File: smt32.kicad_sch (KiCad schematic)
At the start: 3 parts, among them P1 CONN28, P2 CONN28, P3 CONN6

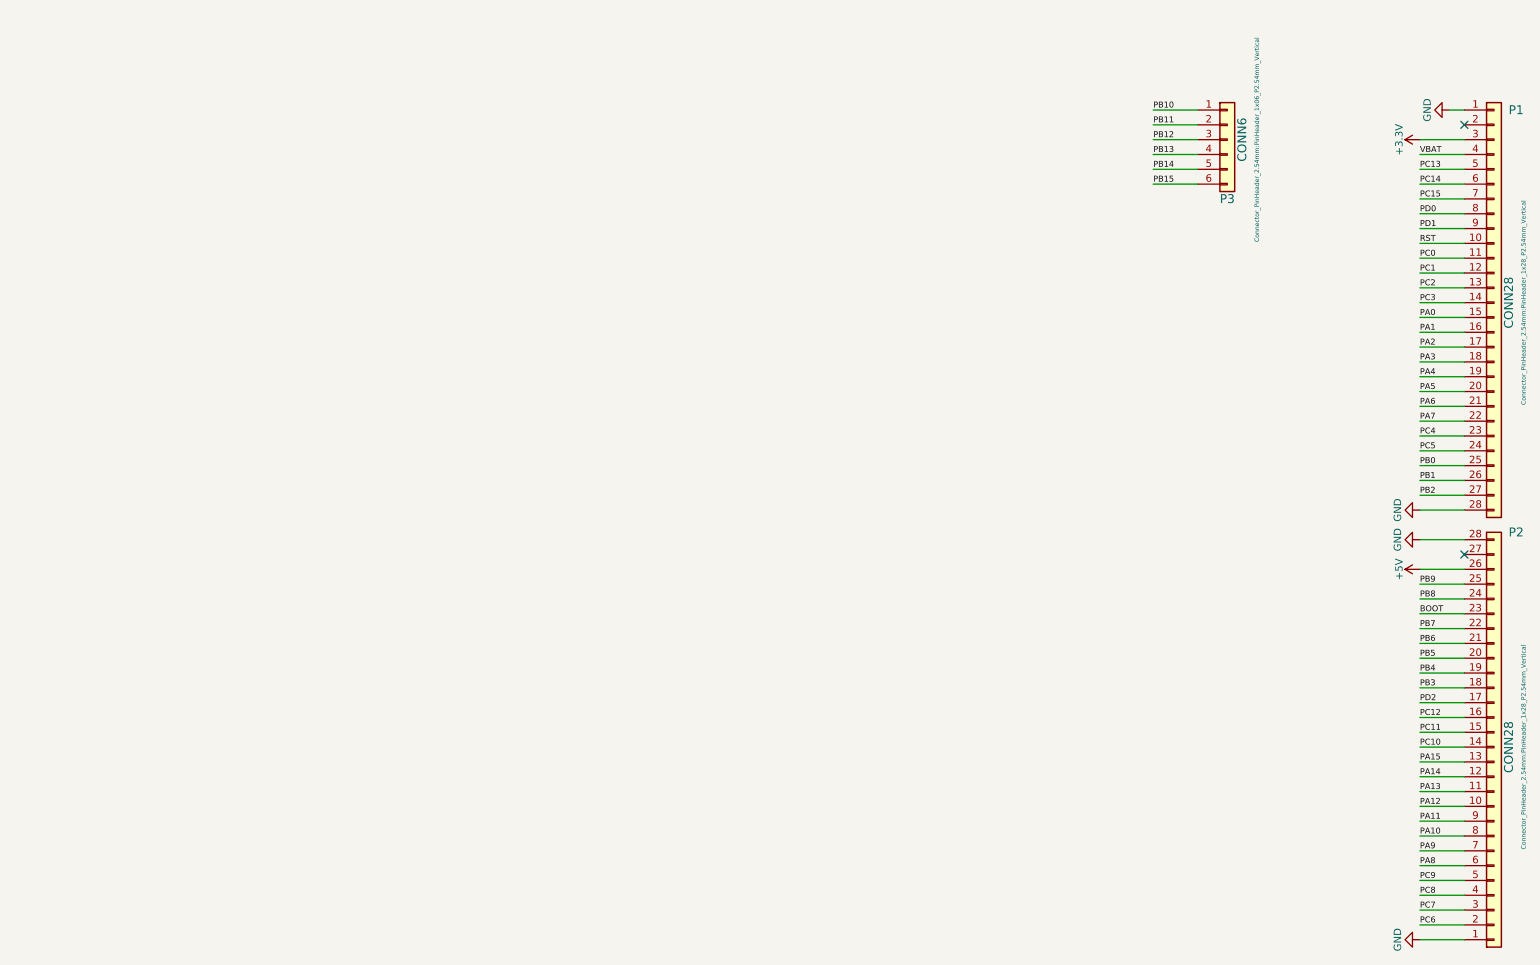
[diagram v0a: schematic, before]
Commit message: adicionado parte de vegulagem de tençaõ 5 -> 3.3v
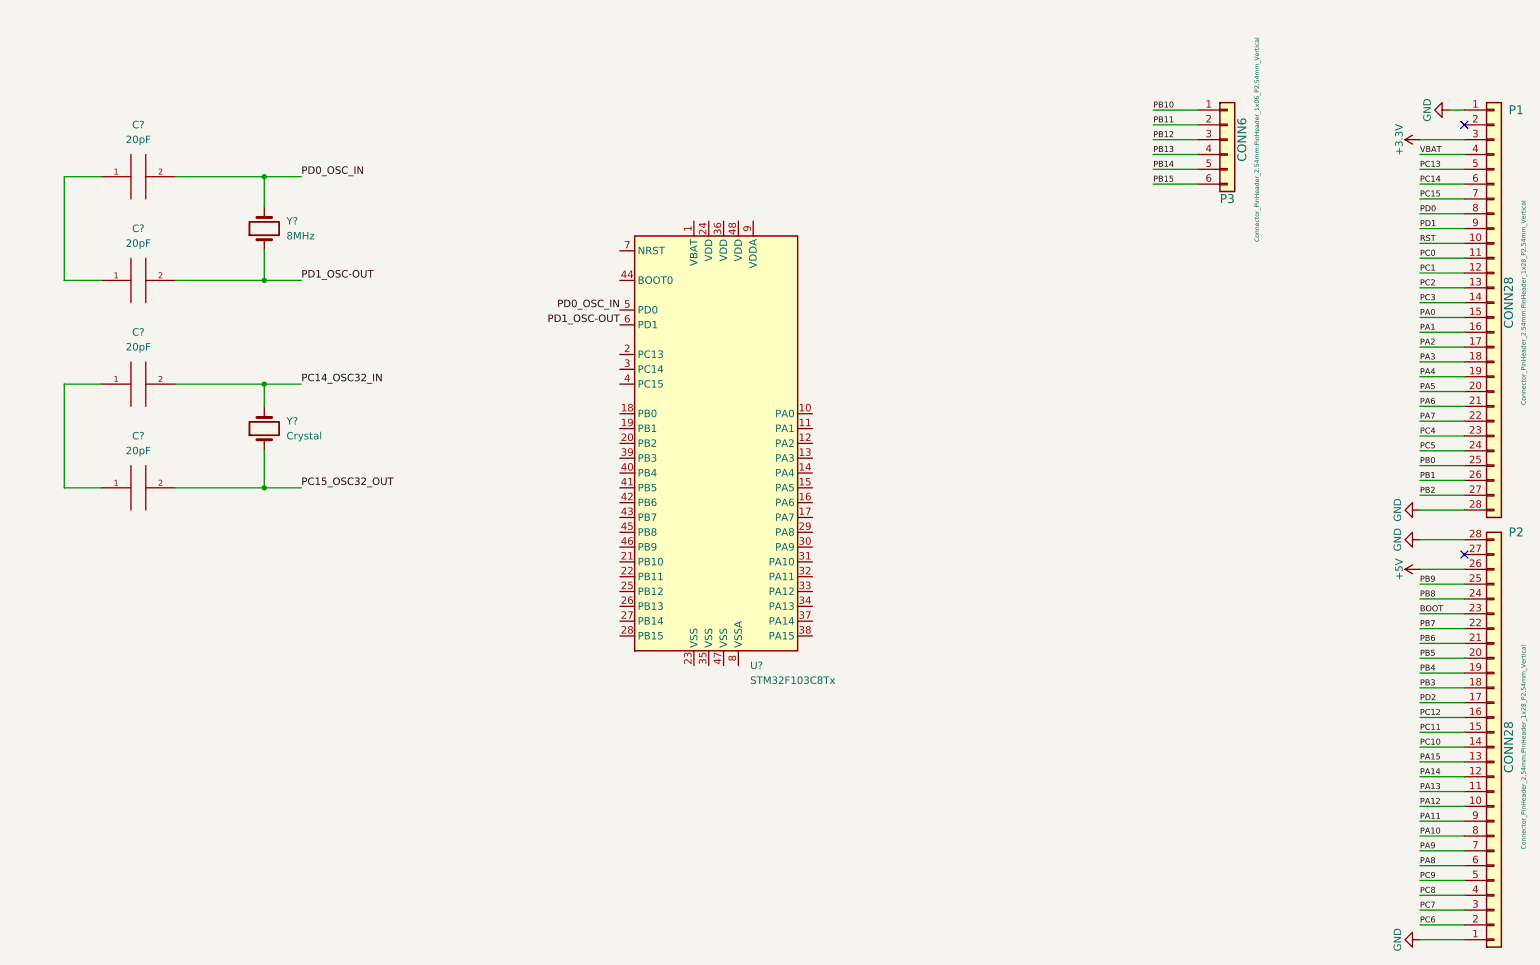
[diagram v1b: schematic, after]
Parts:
- added C? (x4): 20pF, symbol pspice:CAP
- added U?: STM32F103C8Tx, Package_QFP:LQFP-48_7x7mm_P0.5mm, symbol MCU_ST_STM32F1:STM32F103C8Tx
- added Y?: 8MHz, symbol Device:Crystal
- added Y?: Crystal, symbol Device:Crystal
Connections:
- new net: C?.1, C?.1 (x2)
- new net PC14_OSC32_IN: C?.2, Y?.2
- new net PC15_OSC32_OUT: C?.2, Y?.1
- new net PD0_OSC_IN: C?.2, U?.5 (PD0), Y?.2
- new net PD1_OSC-OUT: C?.2, U?.6 (PD1), Y?.1

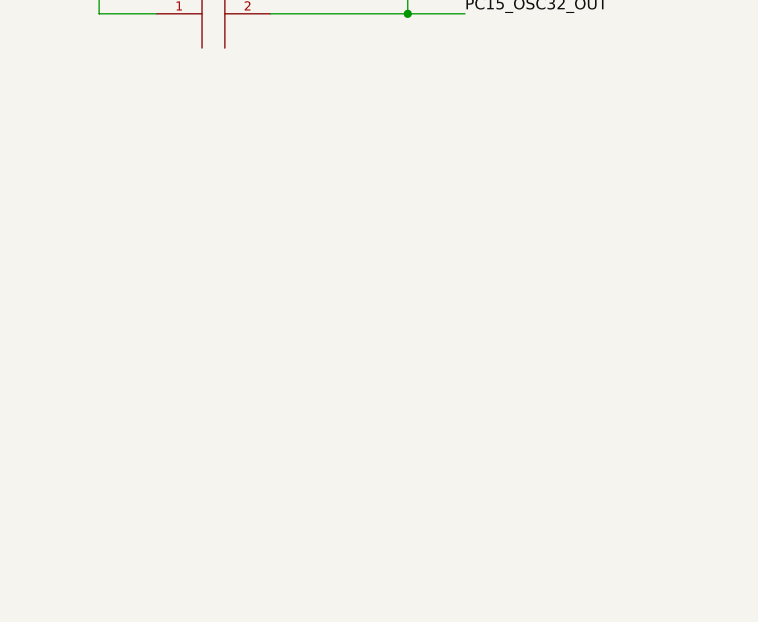
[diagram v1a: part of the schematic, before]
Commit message: adicionado parte de vegulagem de tençaõ 5 -> 3.3v
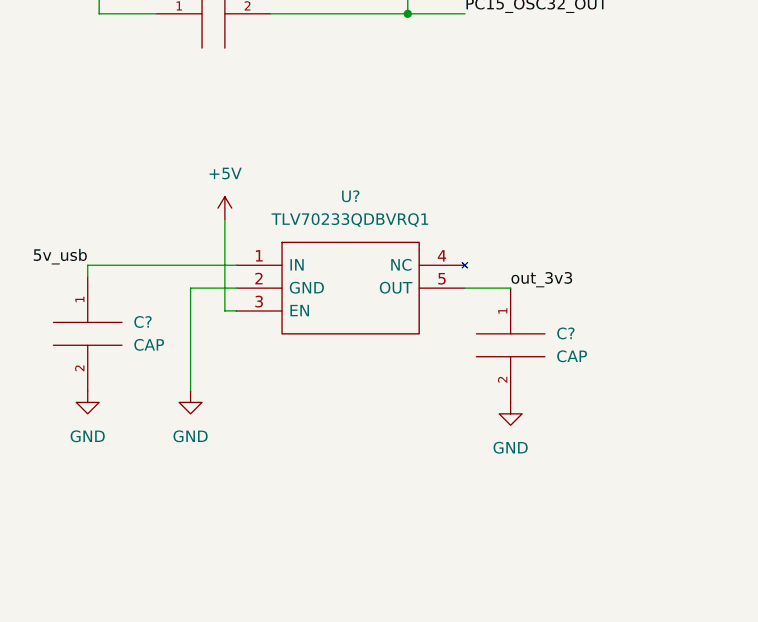
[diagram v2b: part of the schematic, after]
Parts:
- added C? (x2): CAP, symbol pspice:CAP
- added U?: TLV70233QDBVRQ1, SOT95P280X145-5N, symbol TLV70233QDBVRQ1:TLV70233QDBVRQ1
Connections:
- net +5V: now also U?.3 (EN)
- net GND: now also C?.2, C?.2, U?.2 (GND)
- new net 5v_usb: C?.1, U?.1 (IN)
- new net out_3v3: C?.1, U?.5 (OUT)
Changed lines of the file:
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@@
   (no_connect (at 266.7 91.44))
   (no_connect (at 266.7 17.78))
+  (wire (pts (xy 40.64 102.87) (xy 40.64 113.03))
+    (stroke (width 0) (type default) (color 0 0 0 0))
+  )
   (wire (pts (xy 266.7 93.98) (xy 259.08 93.98))
     (stroke (width 0) (type solid) (color 0 0 0 0))
@@
     (stroke (width 0) (type default) (color 0 0 0 0))
   )
+  (wire (pts (xy 25.4 107.95) (xy 25.4 109.22))
+    (stroke (width 0) (type default) (color 0 0 0 0))
+  )
   (wire (pts (xy 266.7 35.56) (xy 259.08 35.56))
     (stroke (width 0) (type solid) (color 0 0 0 0))
@@
     (stroke (width 0) (type solid) (color 0 0 0 0))
   )
+  (wire (pts (xy 41.91 113.03) (xy 40.64 113.03))
+    (stroke (width 0) (type default) (color 0 0 0 0))
+  )
   (wire (pts (xy 45.72 44.45) (xy 60.96 44.45))
     (stroke (width 0) (type default) (color 0 0 0 0))
   )
+  (wire (pts (xy 41.91 110.49) (xy 36.83 110.49))
+    (stroke (width 0) (type default) (color 0 0 0 0))
+  )
   (wire (pts (xy 26.67 80.01) (xy 26.67 62.23))
     (stroke (width 0) (type default) (color 0 0 0 0))
@@
     (stroke (width 0) (type default) (color 0 0 0 0))
   )
+  (wire (pts (xy 41.91 107.95) (xy 25.4 107.95))
+    (stroke (width 0) (type default) (color 0 0 0 0))
+  )
   (wire (pts (xy 26.67 26.67) (xy 26.67 44.45))
     (stroke (width 0) (type default) (color 0 0 0 0))
@@
     (stroke (width 0) (type solid) (color 0 0 0 0))
   )
+  (wire (pts (xy 67.31 110.49) (xy 72.39 110.49))
+    (stroke (width 0) (type default) (color 0 0 0 0))
+  )
   (wire (pts (xy 266.7 101.6) (xy 259.08 101.6))
     (stroke (width 0) (type solid) (color 0 0 0 0))
@@
   (wire (pts (xy 220.98 20.32) (xy 213.36 20.32))
     (stroke (width 0) (type solid) (color 0 0 0 0))
+  )
+  (wire (pts (xy 36.83 110.49) (xy 36.83 121.92))
+    (stroke (width 0) (type default) (color 0 0 0 0))
   )
   (wire (pts (xy 266.7 139.7) (xy 259.08 139.7))
@@
     (effects (font (size 1.016 1.016)) (justify left bottom))
   )
+  (label "out_3v3" (at 72.39 110.49 0)
+    (effects (font (size 1.27 1.27)) (justify left bottom))
+  )
   (label "PA0" (at 259.08 50.8 0)
     (effects (font (size 1.016 1.016)) (justify left bottom))
@@
   (label "PA2" (at 259.08 55.88 0)
     (effects (font (size 1.016 1.016)) (justify left bottom))
+  )
+  (label "5v_usb" (at 25.4 107.95 180)
+    (effects (font (size 1.27 1.27)) (justify right bottom))
   )
   (label "PC5" (at 259.08 73.66 0)
@@
     (pin "1")
   )
+  (symbol (lib_id "power:GND") (at 72.39 123.19 0) (unit 1)
+    (in_bom yes) (on_board yes) (fields_autoplaced)
+    (property "Reference" "#PWR?" (id 0) (at 72.39 129.54 0)
+      (effects (font (size 1.27 1.27)) hide)
+    )
+    (property "Value" "GND" (id 1) (at 72.39 128.27 0))
+    (property "Footprint" "" (id 2) (at 72.39 123.19 0)
+      (effects (font (size 1.27 1.27)) hide)
+    )
+    (property "Datasheet" "" (id 3) (at 72.39 123.19 0)
+      (effects (font (size 1.27 1.27)) hide)
+    )
+    (pin "1")
+  )
+  (symbol (lib_id "pspice:CAP") (at 25.4 115.57 0) (unit 1)
+    (in_bom yes) (on_board yes) (fields_autoplaced)
+    (property "Reference" "C?" (id 0) (at 30.48 114.2999 0)
+      (effects (font (size 1.27 1.27)) (justify left))
+    )
+    (property "Value" "CAP" (id 1) (at 30.48 116.8399 0)
+      (effects (font (size 1.27 1.27)) (justify left))
+    )
+    (property "Footprint" "" (id 2) (at 25.4 115.57 0)
+      (effects (font (size 1.27 1.27)) hide)
+    )
+    (property "Datasheet" "~" (id 3) (at 25.4 115.57 0)
+      (effects (font (size 1.27 1.27)) hide)
+    )
+    (pin "1")
+    (pin "2")
+  )
   (symbol (lib_id "Device:Crystal") (at 60.96 35.56 90) (unit 1)
     (in_bom yes) (on_board yes) (fields_autoplaced)
@@
     (pin "1")
     (pin "2")
+  )
+  (symbol (lib_id "power:GND") (at 36.83 121.92 0) (unit 1)
+    (in_bom yes) (on_board yes) (fields_autoplaced)
+    (property "Reference" "#PWR?" (id 0) (at 36.83 128.27 0)
+      (effects (font (size 1.27 1.27)) hide)
+    )
+    (property "Value" "GND" (id 1) (at 36.83 127 0))
+    (property "Footprint" "" (id 2) (at 36.83 121.92 0)
+      (effects (font (size 1.27 1.27)) hide)
+    )
+    (property "Datasheet" "" (id 3) (at 36.83 121.92 0)
+      (effects (font (size 1.27 1.27)) hide)
+    )
+    (pin "1")
+  )
+  (symbol (lib_id "power:+5V") (at 40.64 102.87 0) (unit 1)
+    (in_bom yes) (on_board yes) (fields_autoplaced)
+    (property "Reference" "#PWR?" (id 0) (at 40.64 106.68 0)
+      (effects (font (size 1.27 1.27)) hide)
+    )
+    (property "Value" "+5V" (id 1) (at 40.64 97.79 0))
+    (property "Footprint" "" (id 2) (at 40.64 102.87 0)
+      (effects (font (size 1.27 1.27)) hide)
+    )
+    (property "Datasheet" "" (id 3) (at 40.64 102.87 0)
+      (effects (font (size 1.27 1.27)) hide)
+    )
+    (pin "1")
   )
   (symbol (lib_id "MCU_ST_STM32F1:STM32F103C8Tx") (at 139.7 72.39 0) (unit 1)
@@
     (pin "9")
   )
+  (symbol (lib_id "TLV70233QDBVRQ1:TLV70233QDBVRQ1") (at 41.91 107.95 0) (unit 1)
+    (in_bom yes) (on_board yes) (fields_autoplaced)
+    (property "Reference" "U?" (id 0) (at 54.61 100.33 0))
+    (property "Value" "TLV70233QDBVRQ1" (id 1) (at 54.61 102.87 0))
+    (property "Footprint" "SOT95P280X145-5N" (id 2) (at 63.5 105.41 0)
+      (effects (font (size 1.27 1.27)) (justify left) hide)
+    )
+    (property "Datasheet" "http://www.ti.com/lit/gpn/tlv702-q1" (id 3) (at 63.5 107.95 0)
+      (effects (font (size 1.27 1.27)) (justify left) hide)
+    )
+    (property "Description" "Automotive 300mA Low-Iq Low-Dropout (LDO) Regulator for Portables" (id 4) (at 63.5 110.49 0)
+      (effects (font (size 1.27 1.27)) (justify left) hide)
+    )
+    (property "Height" "1.45" (id 5) (at 63.5 113.03 0)
+      (effects (font (size 1.27 1.27)) (justify left) hide)
+    )
+    (property "Manufacturer_Name" "Texas Instruments" (id 6) (at 63.5 115.57 0)
+      (effects (font (size 1.27 1.27)) (justify left) hide)
+    )
+    (property "Manufacturer_Part_Number" "TLV70233QDBVRQ1" (id 7) (at 63.5 118.11 0)
+      (effects (font (size 1.27 1.27)) (justify left) hide)
+    )
+    (property "Mouser Part Number" "595-TLV70233QDBVRQ1" (id 8) (at 63.5 120.65 0)
+      (effects (font (size 1.27 1.27)) (justify left) hide)
+    )
+    (property "Mouser Price/Stock" "https://www.mouser.co.uk/ProductDetail/Texas-Instruments/TLV70233QDBVRQ1?qs=W0yvOO0ixfEs6837Pr9aXg%3D%3D" (id 9) (at 63.5 123.19 0)
+      (effects (font (size 1.27 1.27)) (justify left) hide)
+    )
+    (property "Arrow Part Number" "TLV70233QDBVRQ1" (id 10) (at 63.5 125.73 0)
+      (effects (font (size 1.27 1.27)) (justify left) hide)
+    )
+    (property "Arrow Price/Stock" "https://www.arrow.com/en/products/tlv70233qdbvrq1/texas-instruments?region=nac" (id 11) (at 63.5 128.27 0)
+      (effects (font (size 1.27 1.27)) (justify left) hide)
+    )
+    (pin "1")
+    (pin "2")
+    (pin "3")
+    (pin "4")
+    (pin "5")
+  )
   (symbol (lib_id "pspice:CAP") (at 39.37 62.23 90) (unit 1)
     (in_bom yes) (on_board yes) (fields_autoplaced)
@@
     (pin "2")
   )
+  (symbol (lib_id "power:GND") (at 25.4 121.92 0) (unit 1)
+    (in_bom yes) (on_board yes) (fields_autoplaced)
+    (property "Reference" "#PWR?" (id 0) (at 25.4 128.27 0)
+      (effects (font (size 1.27 1.27)) hide)
+    )
+    (property "Value" "GND" (id 1) (at 25.4 127 0))
+    (property "Footprint" "" (id 2) (at 25.4 121.92 0)
+      (effects (font (size 1.27 1.27)) hide)
+    )
+    (property "Datasheet" "" (id 3) (at 25.4 121.92 0)
+      (effects (font (size 1.27 1.27)) hide)
+    )
+    (pin "1")
+  )
   (symbol (lib_id "Device:Crystal") (at 60.96 69.85 90) (unit 1)
     (in_bom yes) (on_board yes) (fields_autoplaced)
@@
     (pin "2")
   )
+  (symbol (lib_id "pspice:CAP") (at 72.39 116.84 0) (unit 1)
+    (in_bom yes) (on_board yes) (fields_autoplaced)
+    (property "Reference" "C?" (id 0) (at 77.47 115.5699 0)
+      (effects (font (size 1.27 1.27)) (justify left))
+    )
+    (property "Value" "CAP" (id 1) (at 77.47 118.1099 0)
+      (effects (font (size 1.27 1.27)) (justify left))
+    )
+    (property "Footprint" "" (id 2) (at 72.39 116.84 0)
+      (effects (font (size 1.27 1.27)) hide)
+    )
+    (property "Datasheet" "~" (id 3) (at 72.39 116.84 0)
+      (effects (font (size 1.27 1.27)) hide)
+    )
+    (pin "1")
+    (pin "2")
+  )
   (symbol (lib_id "pspice:CAP") (at 39.37 26.67 90) (unit 1)
     (in_bom yes) (on_board yes) (fields_autoplaced)
@@
       (reference "#PWR06") (unit 1) (value "+5V") (footprint "")
     )
+    (path "/11e1c15a-3b95-4f19-b922-6f83c6d2d877"
+      (reference "#PWR?") (unit 1) (value "GND") (footprint "")
+    )
+    (path "/2ccbaa3b-05d4-4ae1-b743-a7161742f8f8"
+      (reference "#PWR?") (unit 1) (value "GND") (footprint "")
+    )
+    (path "/30236a99-6841-4a47-8880-5e321e5dfcdf"
+      (reference "#PWR?") (unit 1) (value "+5V") (footprint "")
+    )
+    (path "/9a979715-3280-4522-8bfd-ad305e729ebc"
+      (reference "#PWR?") (unit 1) (value "GND") (footprint "")
+    )
+    (path "/16fb4a52-0916-421e-b6de-5d2c8c931a68"
+      (reference "C?") (unit 1) (value "CAP") (footprint "")
+    )
     (path "/8b069f63-f084-463f-8d9d-051b570bf7df"
       (reference "C?") (unit 1) (value "20pF") (footprint "")
@@
       (reference "C?") (unit 1) (value "20pF") (footprint "")
     )
+    (path "/e6c82083-475d-46fd-ba93-e6f4cfb02c19"
+      (reference "C?") (unit 1) (value "CAP") (footprint "")
+    )
     (path "/f3b97d65-4094-4033-a21c-b930f74b6629"
       (reference "C?") (unit 1) (value "20pF") (footprint "")
@@
       (reference "U?") (unit 1) (value "STM32F103C8Tx") (footprint "Package_QFP:LQFP-48_7x7mm_P0.5mm")
     )
+    (path "/7588ff18-71d7-42b4-a8c1-626f6988fac7"
+      (reference "U?") (unit 1) (value "TLV70233QDBVRQ1") (footprint "SOT95P280X145-5N")
+    )
     (path "/2c836d86-4c09-45cd-bbf2-5361873cdf5e"
